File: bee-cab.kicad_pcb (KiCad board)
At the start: 2 copper layers, 29 x 53.3 mm, 12 parts, among them J1 Conn_01x02_Male, J2 Conn_01x02_Male, J3 Conn_01x02_Male, J4 Conn_01x02_Male

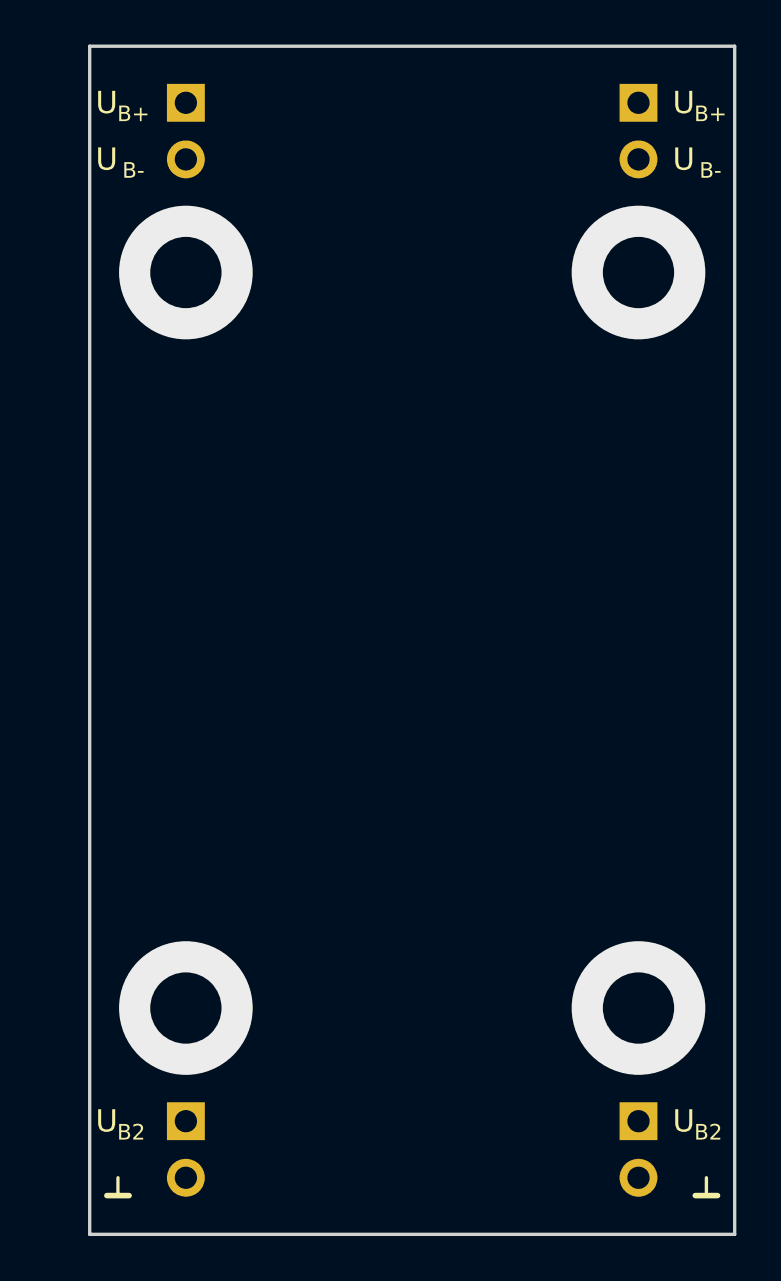
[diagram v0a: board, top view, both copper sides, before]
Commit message: Place parts on PCB.
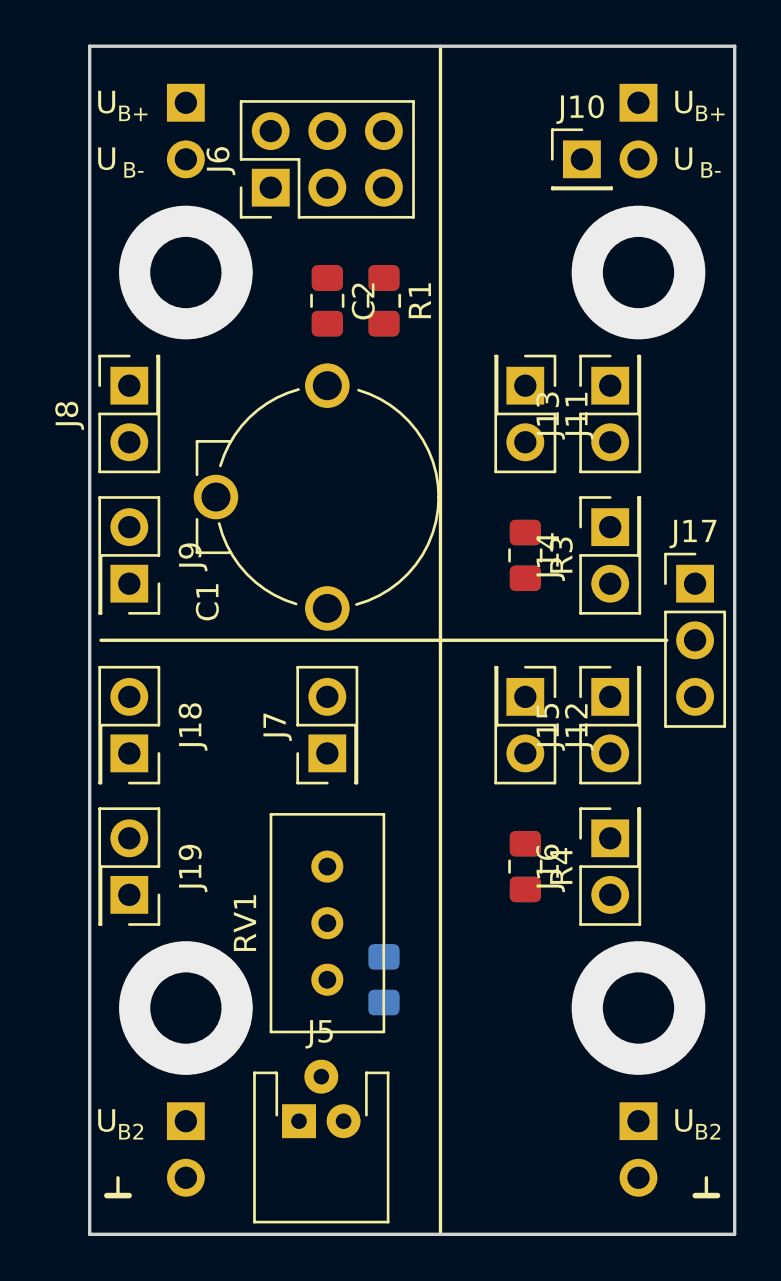
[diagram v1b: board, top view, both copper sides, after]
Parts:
- added C1: C_Variable, Capacitor_THT-emt:C_Trimmer_Vishay_D10mm_Vertical_HolePattern5mmx10mm, F.Cu at (85.1, 104.1)
- added C2: C, Capacitor_SMD:C_0805_2012Metric_Pad1.15x1.40mm_HandSolder, F.Cu at (85.1, 100.3)
- added J10: Conn_01x01, Connector_PinHeader_2.54mm:PinHeader_1x01_P2.54mm_Vertical, F.Cu at (96.5, 94.0)
- added J11: Conn_02x01, Connector_PinHeader_2.54mm:PinHeader_2x01_P2.54mm_Vertical, F.Cu at (94.0, 104.1)
- added J12: Conn_02x01, Connector_PinHeader_2.54mm:PinHeader_2x01_P2.54mm_Vertical, F.Cu at (94.0, 118.1)
- added J13: Conn_01x02, Connector_PinSocket_2.54mm:PinSocket_2x01_P2.54mm_Vertical, F.Cu at (97.8, 104.1)
- added J14: Conn_01x02, Connector_PinSocket_2.54mm:PinSocket_2x01_P2.54mm_Vertical, F.Cu at (97.8, 110.5)
- added J15: Conn_01x02, Connector_PinSocket_2.54mm:PinSocket_2x01_P2.54mm_Vertical, F.Cu at (97.8, 118.1)
- added J16: Conn_01x02, Connector_PinSocket_2.54mm:PinSocket_2x01_P2.54mm_Vertical, F.Cu at (97.8, 124.5)
- added J17: Conn_01x03, Connector_PinHeader_2.54mm:PinHeader_1x03_P2.54mm_Vertical, F.Cu at (101.6, 113.0)
- added J18: Conn_01x02, Connector_PinSocket_2.54mm:PinSocket_2x01_P2.54mm_Vertical, F.Cu at (76.2, 120.7)
- added J19: Conn_01x02, Connector_PinSocket_2.54mm:PinSocket_2x01_P2.54mm_Vertical, F.Cu at (76.2, 127.0)
- added J5: Conn_01x03, Connector_Molex-emt:Molex_Easy-On_528070310_1x03_P1.0mm_Horizontal, F.Cu at (83.8, 137.2)
- added J6: Conn_02x03_Odd_Even, Connector_PinHeader_2.54mm:PinHeader_2x03_P2.54mm_Vertical, F.Cu at (82.5, 95.2)
- added J7: Conn_02x01, Connector_PinHeader_2.54mm:PinHeader_2x01_P2.54mm_Vertical, F.Cu at (85.1, 120.7)
- added J8: Conn_01x02, Connector_PinSocket_2.54mm:PinSocket_2x01_P2.54mm_Vertical, F.Cu at (76.2, 104.1)
- added J9: Conn_01x02, Connector_PinSocket_2.54mm:PinSocket_2x01_P2.54mm_Vertical, F.Cu at (76.2, 113.0)
- added R1: R, Resistor_SMD:R_0805_2012Metric_Pad1.15x1.40mm_HandSolder, F.Cu at (87.6, 100.3)
- added R2: R, Resistor_SMD:R_0805_2012Metric_Pad1.15x1.40mm_HandSolder, B.Cu at (87.6, 130.8)
- added R3: R, Resistor_SMD:R_0805_2012Metric_Pad1.15x1.40mm_HandSolder, F.Cu at (94.0, 111.8)
- added R4: R, Resistor_SMD:R_0805_2012Metric_Pad1.15x1.40mm_HandSolder, F.Cu at (94.0, 125.7)
- added RV1: R_POT, Potentiometer_THT:Potentiometer_Bourns_3296W_Vertical, F.Cu at (85.1, 125.7)
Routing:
- net Net-(R2-Pad1): vias 0 -> 1
- net -15V: vias 0 -> 1
- net (no net): vias 4 -> 2
